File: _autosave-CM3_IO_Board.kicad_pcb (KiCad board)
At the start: 2 copper layers, 93.3 x 116.8 mm, 56 parts, among them J1 Bus_PCI_Express_Mini, J11 USB_A, J2 USB_B_Micro, J3 Conn_02x03_Odd_Even, J4 Conn_02x09_Odd_Even, J5 Conn_01x02, J6 Conn_01x02, J7 Screw_Terminal_01x02, J8 Micro_SD_Card, J9 Conn_01x02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

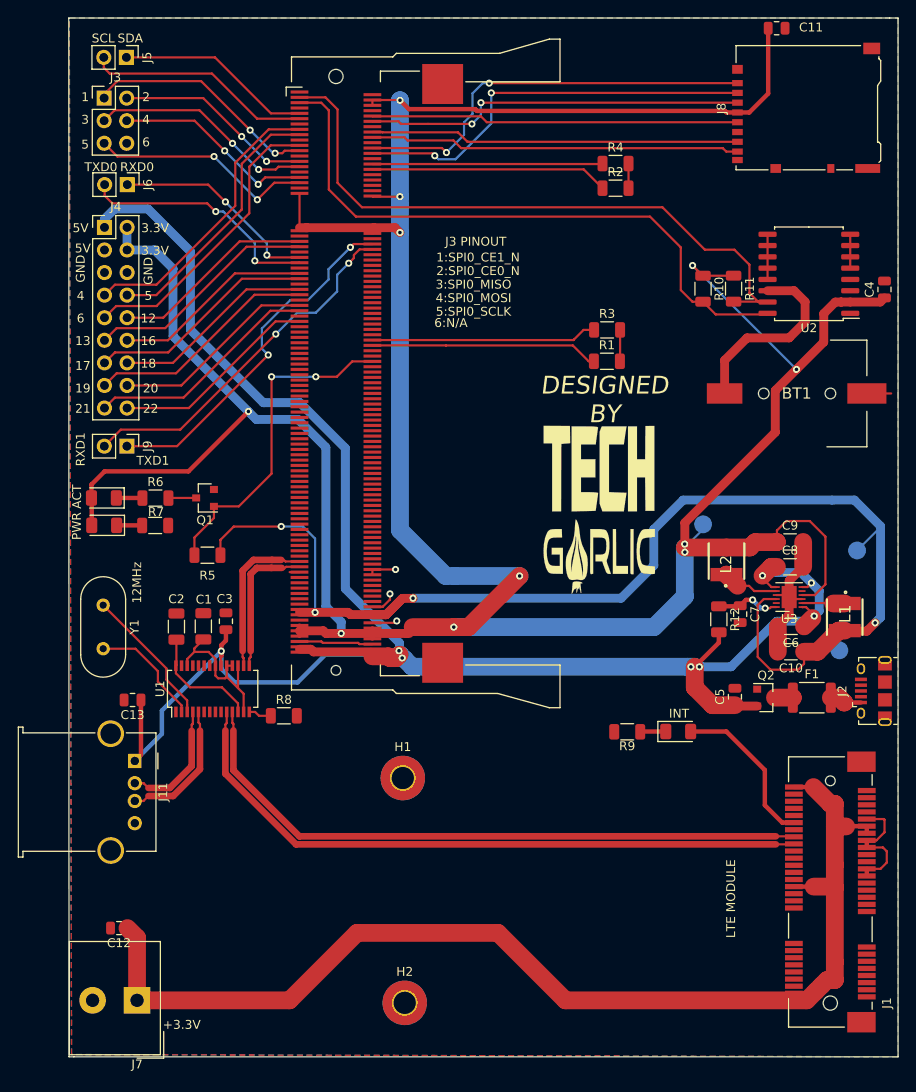
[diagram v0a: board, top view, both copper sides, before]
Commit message: USB pinHeader added
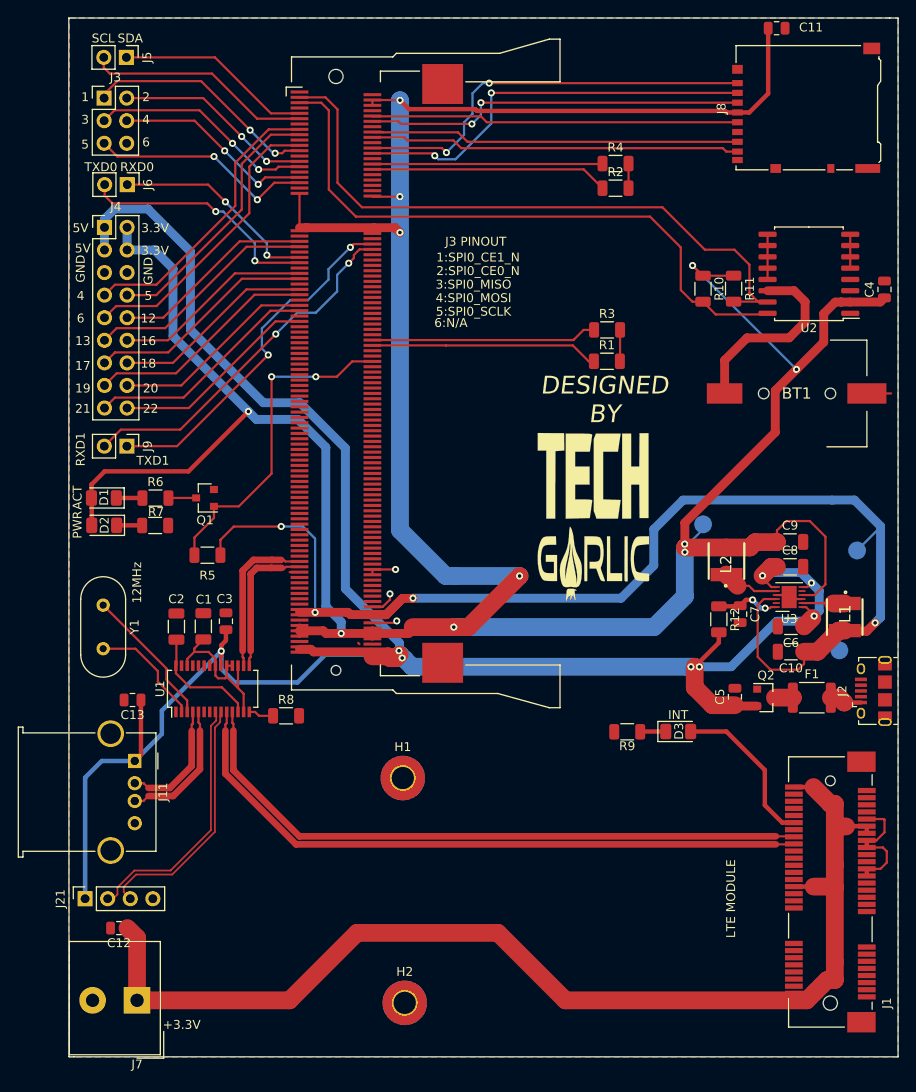
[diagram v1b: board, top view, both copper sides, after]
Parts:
- removed the G*** at (103.4, 86.9)
- removed the G*** at (93.5, 77.2)
- added G***: LOGO, graphics:Front layer logo, B.Cu at (92.7, 76.7)
- added G***: LOGO, graphics:Front layer logo, F.Cu at (102.7, 87.7)
- added J21: Conn_01x04, Connector_PinSocket_2.54mm:PinSocket_1x04_P2.54mm_Vertical, F.Cu at (45.7, 130.8)
- moved R8 0.25 mm to (68.3, 110.2)
- renumbered ACT to D1, PWR to D2, INT to D3
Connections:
- U1 pad 8: Net-(U1-Pad8) -> TP_N
- U1 pad 9: Net-(U1-Pad9) -> TP_P
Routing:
- net TP_N: track 0.00 -> 28.8 mm
- net TP_P: track 0.00 -> 28.2 mm
- net +5V: track 218.8 -> 241.3 mm
- net GND: track 67.6 -> 45.9 mm
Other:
- board text added: "ACT"
- board text added: "INT"
- board text added: "PWR"
